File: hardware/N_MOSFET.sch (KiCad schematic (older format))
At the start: 4 parts, among them Q1 Q_NMOS_DGS

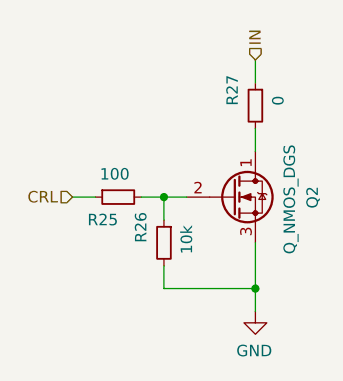
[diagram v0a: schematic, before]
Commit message: 1. added 2X20 connector, \n 2. changed the footprints of schootkies and zenner diodes to a bigger ones, \n 3. changed pcb layout entirely couse duck me, that connector i too duking BIG.
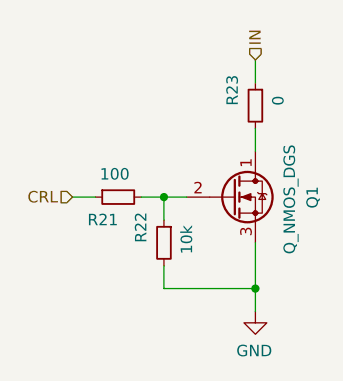
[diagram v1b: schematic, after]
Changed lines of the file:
@@
 $Descr A4 11693 8268
 encoding utf-8
-Sheet 17 20
+Sheet 16 20
 Title ""
 Date ""
@@
 AR Path="/625EC444/61F87DF2" Ref="Q4"  Part="1"
 AR Path="/6262347B/61F87DF2" Ref="Q5"  Part="1"
-F 0 "Q2" V 6700 4000 50  0000 L CNN
+F 0 "Q1" V 6700 4000 50  0000 L CNN
 F 1 "Q_NMOS_DGS" V 6600 3800 50  0000 L CNN
 F 2 "Package_TO_SOT_SMD:SOT-23" H 6550 4150 50  0001 C CNN
@@
 AR Path="/625EC444/61F87DFA" Ref="R32"  Part="1"
 AR Path="/6262347B/61F87DFA" Ref="R35"  Part="1"
-F 0 "R26" V 6150 4250 50  0000 L CNN
+F 0 "R22" V 6150 4250 50  0000 L CNN
 F 1 "10k" V 5950 4200 50  0000 L CNN
 F 2 "Resistor_SMD:R_0603_1608Metric" H 6050 4250 50  0001 C CNN
@@
 AR Path="/625EC444/61F87E05" Ref="R31"  Part="1"
 AR Path="/6262347B/61F87E05" Ref="R34"  Part="1"
-F 0 "R25" V 5950 4050 50  0000 L CNN
+F 0 "R21" V 5950 4050 50  0000 L CNN
 F 1 "100" V 5750 4000 50  0000 L CNN
 F 2 "Resistor_SMD:R_0603_1608Metric" H 5850 4050 50  0001 C CNN
@@
 AR Path="/625EC444/61F87E0C" Ref="R33"  Part="1"
 AR Path="/6262347B/61F87E0C" Ref="R36"  Part="1"
-F 0 "R27" V 6550 3650 50  0000 L CNN
+F 0 "R23" V 6550 3650 50  0000 L CNN
 F 1 "0" V 6350 3650 50  0000 L CNN
 F 2 "Resistor_SMD:R_0603_1608Metric" H 6450 3650 50  0001 C CNN
@@
 AR Path="/625EC444/61F87E13" Ref="#PWR0125"  Part="1"
 AR Path="/6262347B/61F87E13" Ref="#PWR0126"  Part="1"
-F 0 "#PWR0107" H 6450 4300 50  0001 C CNN
+F 0 "#PWR0126" H 6450 4300 50  0001 C CNN
 F 1 "GND" H 6455 4377 50  0000 C CNN
 F 2 "" H 6450 4550 50  0001 C CNN

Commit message: Updated to be compatible with KiCad 6.0.0, changed chematics layouts to fit in A4 worksheet and finished routing the rest of the signals.
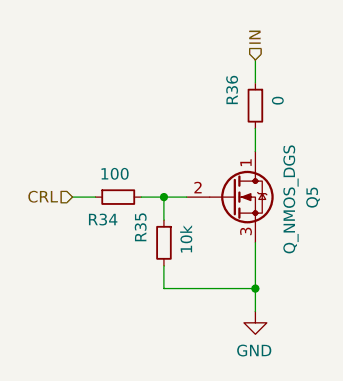
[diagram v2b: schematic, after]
